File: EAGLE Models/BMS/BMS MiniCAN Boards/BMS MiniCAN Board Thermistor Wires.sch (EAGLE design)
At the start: 74 parts, among them IC1 AT90CAN128, IC2 MCP2551SO8, IC3 NUP2105L, IC5 FT232RL, Q1 56P2859, X2 6_PIN_CONNMOLEX_HORI, X3 6_PIN_CONNMOLEX_HORI, X4 6_PIN_CONNMOLEX_HORI, X5 6_PIN_CONNMOLEX_HORI, X6 6_PIN_CONNMOLEX_HORI

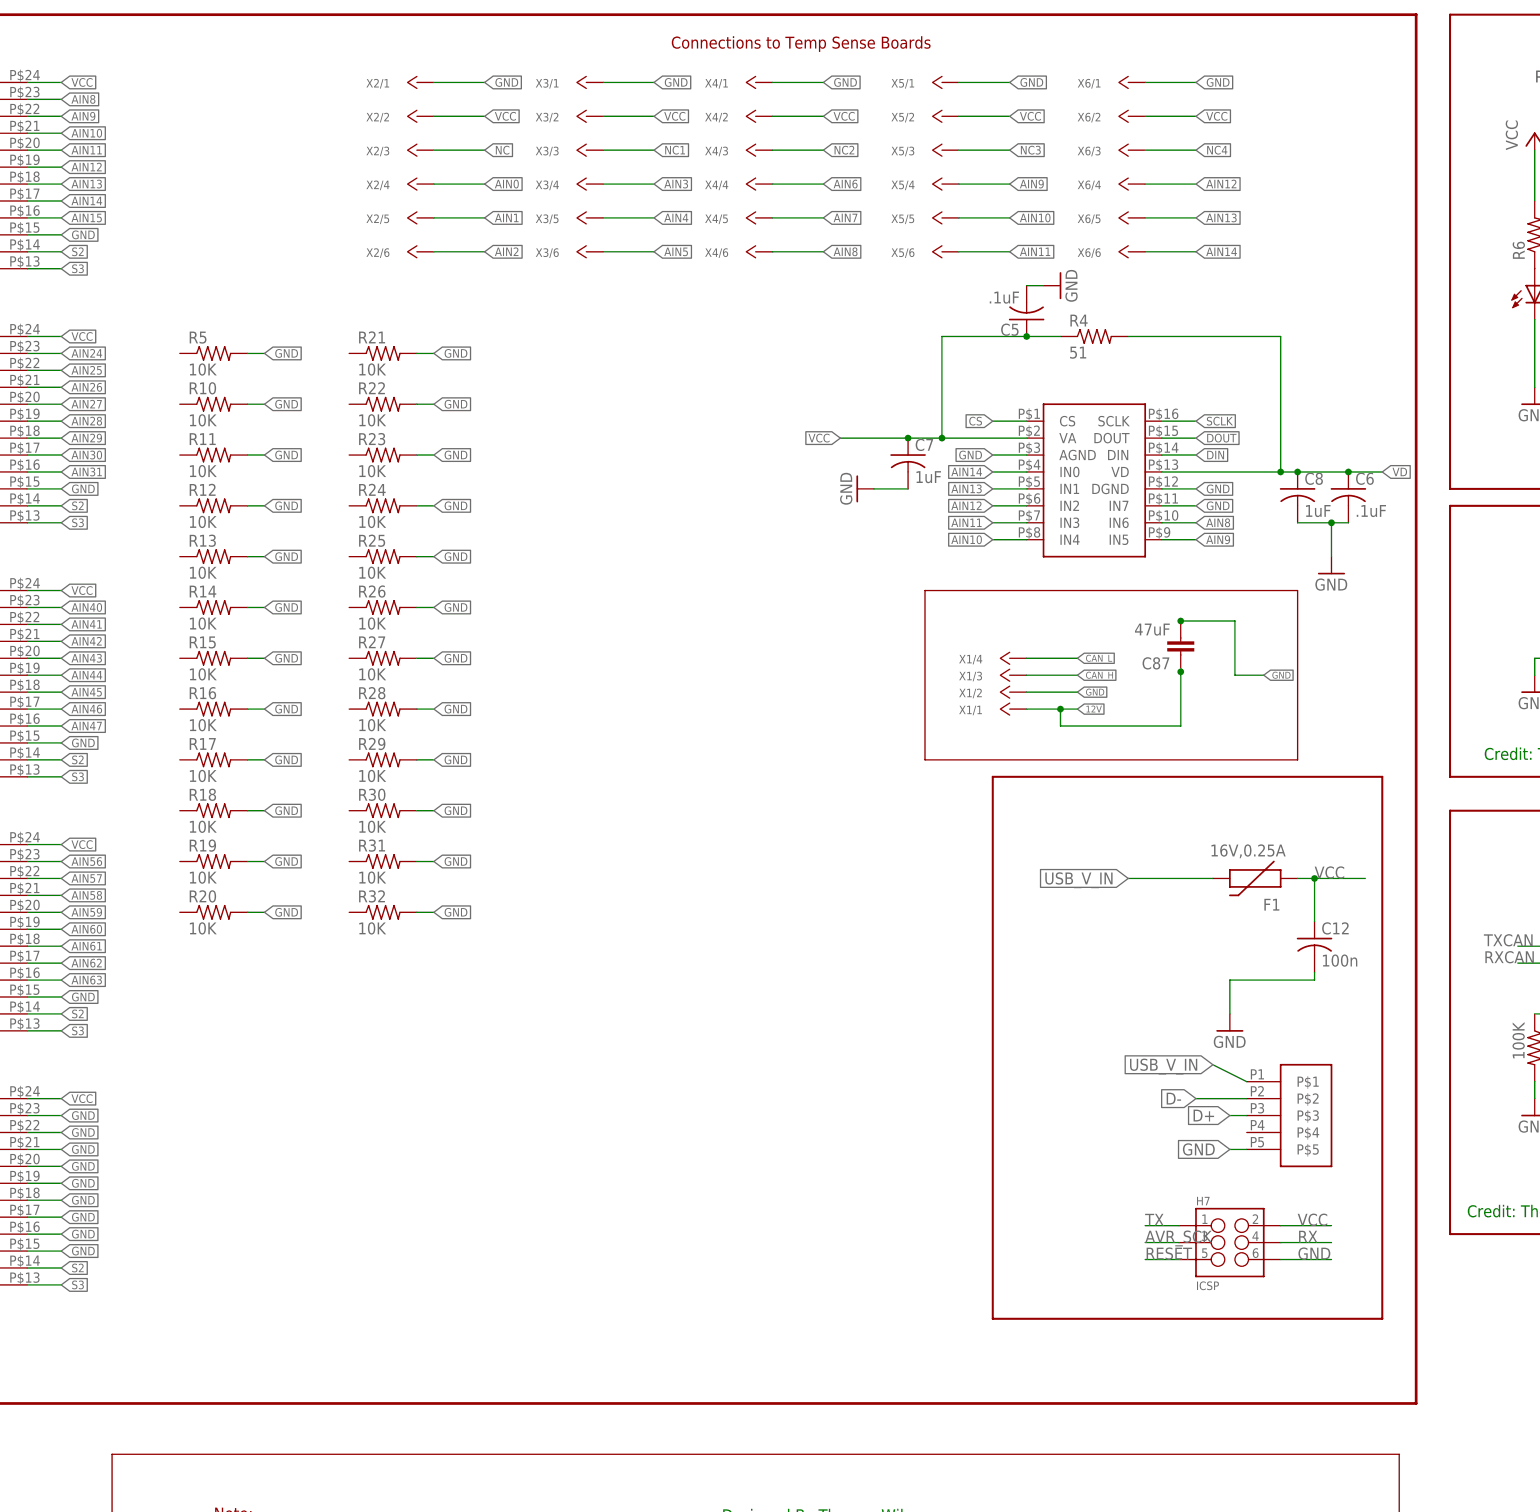
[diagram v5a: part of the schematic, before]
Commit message: Connected thermistor connectors and general cleanup
Connected the thermistor connectors to the muxes and fixed some issues
with the connector itself. Also deleted the old ADC.
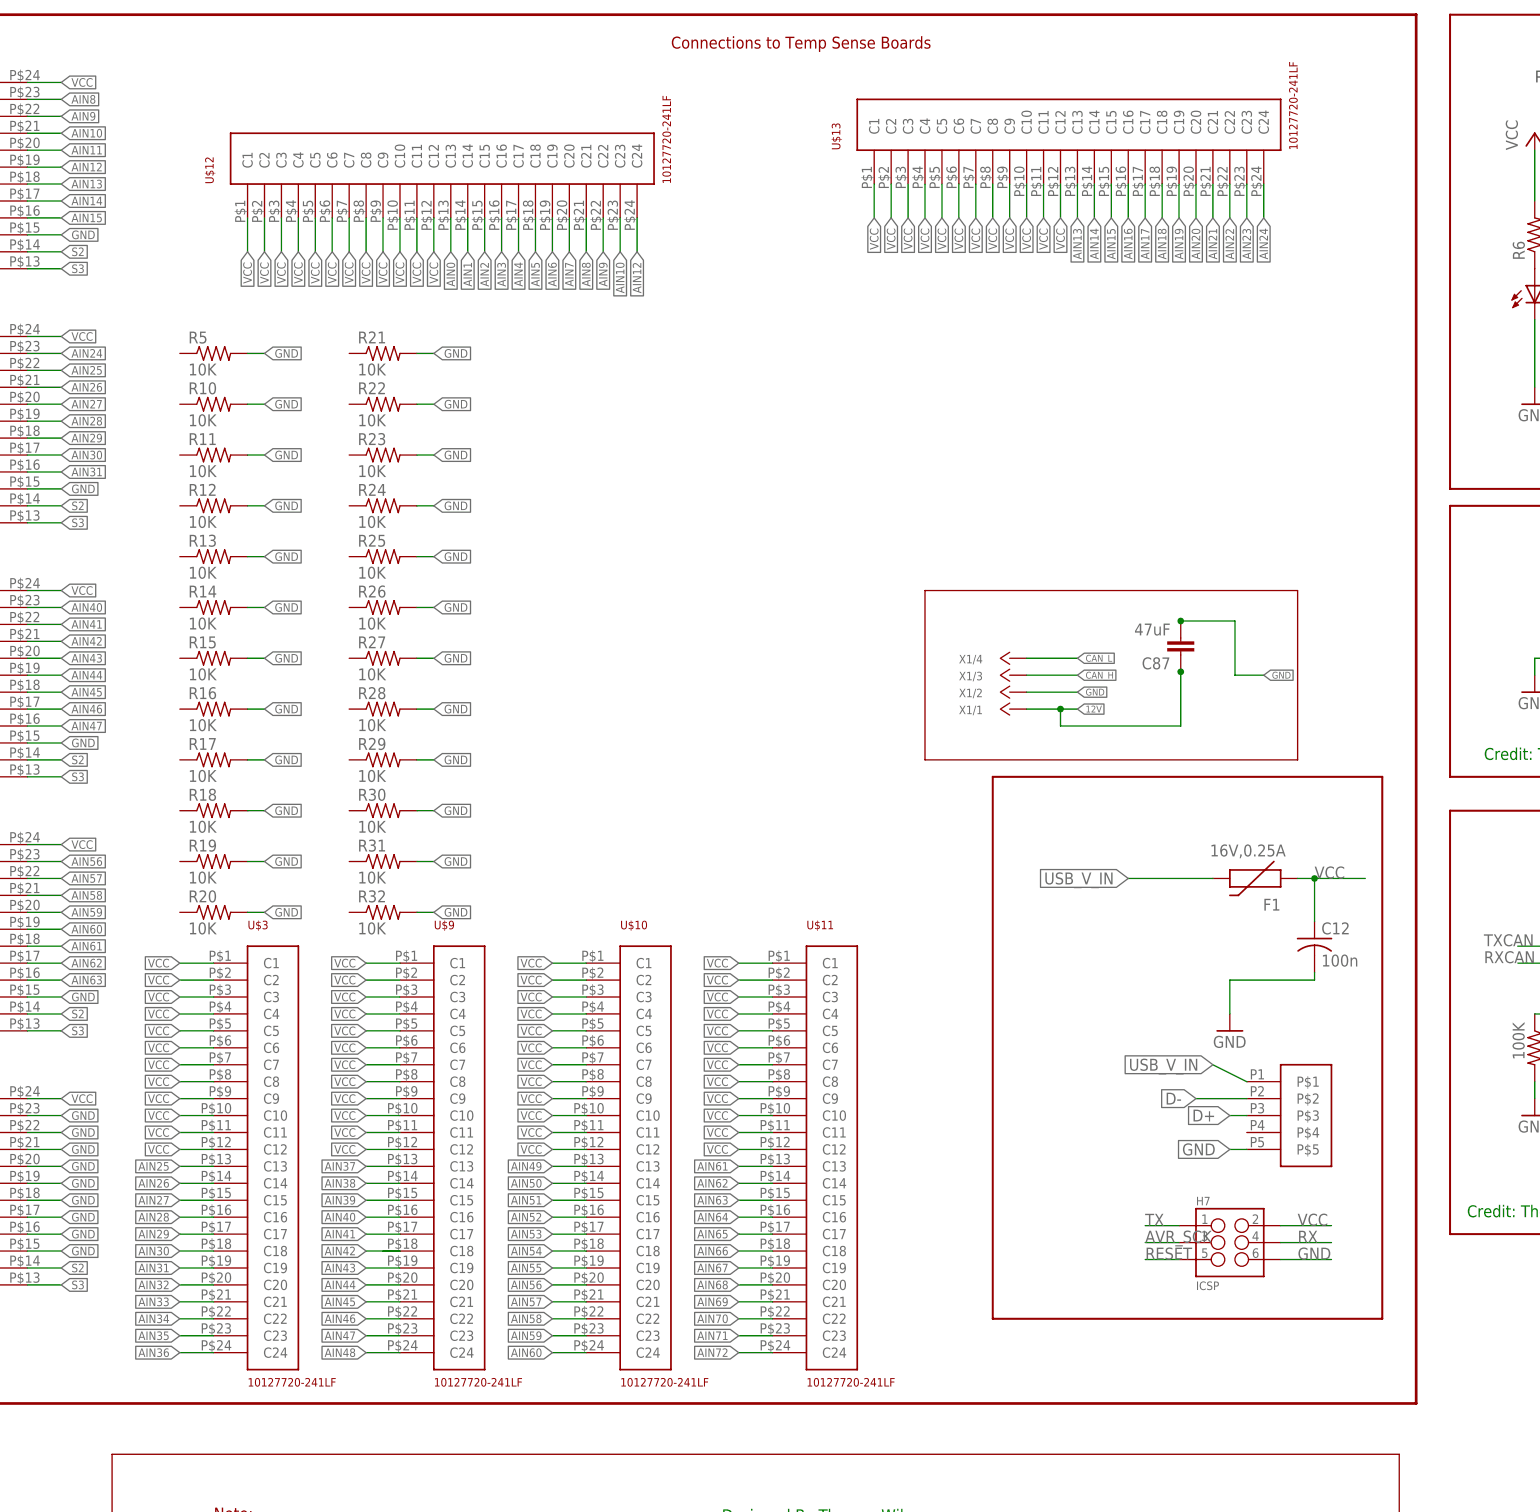
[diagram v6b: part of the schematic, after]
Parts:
- removed C5, C6: .1uF, rcl:C-USC0805
- removed C7, C8: 1uF, rcl:C-USC0805
- removed R4: 51, adafruit:R-US_R0805
- removed U$2: ADC084S101, BMS Lbr:ADC084S101
- removed X2, X3, X4, X5, X6: 6_PIN_CONNMOLEX_HORI, BMS Lbr:6_PIN_CONNMOLEX_HORI
- added U$10, U$11, U$12, U$13, U$3, U$9: 10127720-241LF, con-amphenol:10127720-241LF
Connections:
- removed net NC: X2/3.$/1
- removed net NC1: X3/3.$/1
- removed net NC2: X4/3.$/1
- removed net NC3: X5/3.$/1
- removed net NC4: X6/3.$/1
- removed net VD: C6.1, C8.1, R4.2, U$2.VD
- new net AIN72: U$11.C24
- net AIN0: now also U$12.C13; no longer X2/4.$/1
- net AIN1: now also U$12.C14; no longer X2/5.$/1
- net AIN10: now also U$12.C23; no longer U$2.IN4, X5/5.$/1
- net AIN11: no longer U$2.IN3, X5/6.$/1
- net AIN12: now also U$12.C24; no longer U$2.IN2, X6/4.$/1
- net AIN13: now also U$13.C13; no longer U$2.IN1, X6/5.$/1
- net AIN14: now also U$13.C14; no longer U$2.IN0, X6/6.$/1
- net AIN15: now also U$13.C15
- net AIN16: now also U$13.C16
- net AIN17: now also U$13.C17
- net AIN18: now also U$13.C18
- net AIN19: now also U$13.C19
- net AIN2: now also U$12.C15; no longer X2/6.$/1
- net AIN20: now also U$13.C20
- net AIN21: now also U$13.C21
- net AIN22: now also U$13.C22
- net AIN23: now also U$13.C23
- net AIN24: now also U$13.C24
- net AIN25: now also U$3.C13
- net AIN26: now also U$3.C14
- net AIN27: now also U$3.C15
- net AIN28: now also U$3.C16
- net AIN29: now also U$3.C17
- net AIN3: now also U$12.C16; no longer X3/4.$/1
- net AIN30: now also U$3.C18
- net AIN31: now also U$3.C19
- net AIN32: now also U$3.C20
- net AIN33: now also U$3.C21
- net AIN34: now also U$3.C22
- net AIN35: now also U$3.C23
- net AIN36: now also U$3.C24
- net AIN37: now also U$9.C13
- net AIN38: now also U$9.C14
- net AIN39: now also U$9.C15
- net AIN4: now also U$12.C17; no longer X3/5.$/1
- net AIN40: now also U$9.C16
- net AIN41: now also U$9.C17
- net AIN42: now also U$9.C18
- net AIN43: now also U$9.C19
- net AIN44: now also U$9.C20
- net AIN45: now also U$9.C21
- net AIN46: now also U$9.C22
- net AIN47: now also U$9.C23
- net AIN48: now also U$9.C24
- net AIN49: now also U$10.C13
- net AIN5: now also U$12.C18; no longer X3/6.$/1
- net AIN50: now also U$10.C14
- net AIN51: now also U$10.C15
- net AIN52: now also U$10.C16
- net AIN53: now also U$10.C17
- net AIN54: now also U$10.C18
- net AIN55: now also U$10.C19
- net AIN56: now also U$10.C20
- net AIN57: now also U$10.C21
- net AIN58: now also U$10.C22
- net AIN59: now also U$10.C23
- net AIN6: now also U$12.C19; no longer X4/4.$/1
- net AIN60: now also U$10.C24
- net AIN61: now also U$11.C13
- net AIN62: now also U$11.C14
- net AIN63: now also U$11.C15
- net AIN64: now also U$11.C16
- net AIN65: now also U$11.C17
- net AIN66: now also U$11.C18
- net AIN67: now also U$11.C19
- net AIN68: now also U$11.C20
- net AIN69: now also U$11.C21
- net AIN7: now also U$12.C20; no longer X4/5.$/1
- net AIN70: now also U$11.C22
- net AIN71: now also U$11.C23
- net AIN8: now also U$12.C21; no longer U$2.IN6, X4/6.$/1
- net AIN9: now also U$12.C22; no longer U$2.IN5, X5/4.$/1
- net CS: no longer U$2.CS
- net DIN: no longer U$2.DIN
- net DOUT: no longer U$2.DOUT
- net GND: no longer C5.2, C6.2, C7.2, C8.2, U$2.AGND, U$2.DGND, U$2.IN7, X2/1.$/1, X3/1.$/1, X4/1.$/1, X5/1.$/1, X6/1.$/1
- net SCLK: no longer U$2.SCLK
- net VCC: now also U$10.C1, U$10.C10, U$10.C11, U$10.C12, U$10.C2, U$10.C3, U$10.C4, U$10.C5, U$10.C6, U$10.C7, U$10.C8, U$10.C9, U$11.C1, U$11.C10, U$11.C11, U$11.C12, U$11.C2, U$11.C3, U$11.C4, U$11.C5, U$11.C6, U$11.C7, U$11.C8, U$11.C9, U$12.C1, U$12.C10, U$12.C11, U$12.C12, U$12.C2, U$12.C3, U$12.C4, U$12.C5, U$12.C6, U$12.C7, U$12.C8, U$12.C9, U$13.C1, U$13.C10, U$13.C11, U$13.C12, U$13.C2, U$13.C3, U$13.C4, U$13.C5, U$13.C6, U$13.C7, U$13.C8, U$13.C9, U$3.C1, U$3.C10, U$3.C11, U$3.C12, U$3.C2, U$3.C3, U$3.C4, U$3.C5, U$3.C6, U$3.C7, U$3.C8, U$3.C9, U$9.C1, U$9.C10, U$9.C11, U$9.C12, U$9.C2, U$9.C3, U$9.C4, U$9.C5, U$9.C6, U$9.C7, U$9.C8, U$9.C9; no longer C5.1, C7.1, R4.1, U$2.VA, X2/2.$/1, X3/2.$/1, X4/2.$/1, X5/2.$/1, X6/2.$/1

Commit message: Connected connectors and thermistors to mux
Connected all the connectors and thermistors to each other, as well as
to the muxes and to the voltage divider resistors.
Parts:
- added R33, R34, R35, R36, R37, R38, R39, R4, R40, R41, R42, R43, R44, R45, R46, R47, R48, R49, R50, R51, R52, R53, R54, R55, R56, R57, R58, R59, R60, R61, R62, R63, R64, R65, R66, R67, R68, R69, R70, R71, R72, R73, R74, R75, R76, R77, R78, R79: 10K, adafruit:R-US_R0603
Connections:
- removed net AIN72: U$11.C24
- removed net CS: IC1.(A12)PC4
- removed net DIN: IC1.(A15/CLKO)PC7
- removed net DOUT: IC1.(A14)PC6
- removed net SCLK: IC1.(A13)PC5
- net AIN0: now also R55.1
- net AIN1: now also R54.1
- net AIN10: now also R13.1
- net AIN11: now also R14.1, U$12.C24, U$4.I12
- net AIN12: now also R15.1, U$13.C13; no longer U$12.C24, U$4.I12
- net AIN13: now also R16.1, U$13.C14; no longer U$13.C13
- net AIN14: now also R17.1, U$13.C15; no longer U$13.C14
- net AIN15: now also R18.1, U$13.C16; no longer U$13.C15
- net AIN16: now also R19.1, U$13.C17; no longer U$13.C16
- net AIN17: now also R20.1, U$13.C18; no longer U$13.C17
- net AIN18: now also R4.1, U$13.C19; no longer U$13.C18
- net AIN19: now also R42.1, U$13.C20; no longer U$13.C19
- net AIN2: now also R53.1
- net AIN20: now also R43.1, U$13.C21; no longer U$13.C20
- net AIN21: now also R44.1, U$13.C22; no longer U$13.C21
- net AIN22: now also R45.1, U$13.C23; no longer U$13.C22
- net AIN23: now also R46.1, U$13.C24; no longer U$13.C23
- net AIN24: now also R49.1, U$3.C13; no longer U$13.C24
- net AIN25: now also R31.1, U$3.C14; no longer U$3.C13
- net AIN26: now also R32.1, U$3.C15; no longer U$3.C14
- net AIN27: now also R33.1, U$3.C16; no longer U$3.C15
- net AIN28: now also R34.1, U$3.C17; no longer U$3.C16
- net AIN29: now also R35.1, U$3.C18; no longer U$3.C17
- net AIN3: now also R52.1
- net AIN30: now also R36.1, U$3.C19; no longer U$3.C18
- net AIN31: now also R37.1, U$3.C20; no longer U$3.C19
- net AIN32: now also R38.1, U$3.C21; no longer U$3.C20
- net AIN33: now also R39.1, U$3.C22; no longer U$3.C21
- net AIN34: now also R40.1, U$3.C23; no longer U$3.C22
- net AIN35: now also R41.1, U$3.C24; no longer U$3.C23
- net AIN36: now also R61.1, U$9.C13; no longer U$3.C24
- net AIN37: now also R60.1, U$9.C14; no longer U$9.C13
- net AIN38: now also R59.1, U$9.C15; no longer U$9.C14
- net AIN39: now also R58.1, U$9.C16; no longer U$9.C15
- net AIN4: now also R51.1
- net AIN40: now also R57.1, U$9.C17; no longer U$9.C16
- net AIN41: now also R56.1, U$9.C18; no longer U$9.C17
- net AIN42: now also R21.1, U$9.C19; no longer U$9.C18
- net AIN43: now also R22.1, U$9.C20; no longer U$9.C19
- net AIN44: now also R23.1, U$9.C21; no longer U$9.C20
- net AIN45: now also R24.1, U$9.C22; no longer U$9.C21
- net AIN46: now also R25.1, U$9.C23; no longer U$9.C22
- net AIN47: now also R26.1, U$9.C24; no longer U$9.C23
- net AIN48: now also R29.1, U$10.C13; no longer U$9.C24
- net AIN49: now also R30.1, U$10.C14; no longer U$10.C13
- net AIN5: now also R50.1
- net AIN50: now also R27.1, U$10.C15; no longer U$10.C14
- net AIN51: now also R28.1, U$10.C16; no longer U$10.C15
- net AIN52: now also R47.1, U$10.C17; no longer U$10.C16
- net AIN53: now also R48.1, U$10.C18; no longer U$10.C17
- net AIN54: now also R62.1, U$10.C19; no longer U$10.C18
- net AIN55: now also R63.1, U$10.C20; no longer U$10.C19
- net AIN56: now also R64.1, U$10.C21; no longer U$10.C20
- net AIN57: now also R65.1, U$10.C22; no longer U$10.C21
- net AIN58: now also R66.1, U$10.C23; no longer U$10.C22
- net AIN59: now also R67.1, U$10.C24; no longer U$10.C23
- net AIN6: now also R5.1
- net AIN60: now also R68.1, U$11.C13; no longer U$10.C24
- net AIN61: now also R69.1, U$11.C14; no longer U$11.C13
- net AIN62: now also R70.1, U$11.C15; no longer U$11.C14
- net AIN63: now also R71.1, U$11.C16; no longer U$11.C15
- net AIN64: now also R72.1, U$11.C17; no longer U$11.C16
- net AIN65: now also R73.1, U$11.C18; no longer U$11.C17
- net AIN66: now also R74.1, U$11.C19; no longer U$11.C18
- net AIN67: now also R75.1, U$11.C20; no longer U$11.C19
- net AIN68: now also R76.1, U$11.C21; no longer U$11.C20
- net AIN69: now also R77.1, U$11.C22; no longer U$11.C21
- net AIN7: now also R10.1
- net AIN70: now also R78.1, U$11.C23; no longer U$11.C22
- net AIN71: now also R79.1, U$11.C24; no longer U$11.C23
- net AIN8: now also R11.1
- net AIN9: now also R12.1
- net GND: now also R33.2, R34.2, R35.2, R36.2, R37.2, R38.2, R39.2, R4.2, R40.2, R41.2, R42.2, R43.2, R44.2, R45.2, R46.2, R47.2, R48.2, R49.2, R50.2, R51.2, R52.2, R53.2, R54.2, R55.2, R56.2, R57.2, R58.2, R59.2, R60.2, R61.2, R62.2, R63.2, R64.2, R65.2, R66.2, R67.2, R68.2, R69.2, R70.2, R71.2, R72.2, R73.2, R74.2, R75.2, R76.2, R77.2, R78.2, R79.2
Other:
- moved on the sheet: C87, R10, R11, R12, R13, R14, R15, R16, R17, R18, R19, R20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
